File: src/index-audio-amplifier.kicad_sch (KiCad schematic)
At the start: 0 parts

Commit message: Add & associate `compact-title-block` submodule
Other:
- title: (none) -> Index Audio Amplifier
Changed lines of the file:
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@@
 	(generator_version "9.0")
 	(paper "A4")
+	(title_block
+		(title "Index Audio Amplifier")
+		(date "In-Progress")
+		(rev "0-dev")
+		(comment 1 "Peter S. Hollander")
+		(comment 2 "recursivenomad@protonmail.com")
+		(comment 3 "MIT-0 OR CC0-1.0")
+		(comment 4 "https://gitlab.com/recursivenomad/index-audio-amplifier/")
+	)
 	(sheet_instances
 		(path "/"

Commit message: Recreate Pico schematic (ignoring connectors)
<https://datasheets.raspberrypi.com/pico/pico-datasheet.pdf#pico-schematic-diagram>
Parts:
- added C1, C2: 47u, Capacitor_SMD:C_0805_2012Metric, symbol Device:C
- added C10, C11, C4, C5, C6, C7, C8, C9: 100n, Capacitor_SMD:C_0603_1608Metric, symbol Device:C
- added C12, C13, C14: 2u2, Capacitor_SMD:C_01005_0402Metric, symbol Device:C
- added C15: 100n, Capacitor_SMD:C_0402_1005Metric, symbol Device:C
- added C16, C17: 15p, Capacitor_SMD:C_0603_1608Metric, symbol Device:C
- added C18: 2u2, Capacitor_SMD:C_0402_1005Metric, symbol Device:C
- added C3: 1n, Capacitor_SMD:C_0603_1608Metric, symbol Device:C
- added D1: MBR120VLSFT1G, Diode_SMD:D_SOD-123F, symbol Diode:MBR1020VL
- added D2: Green, symbol Device:LED
- added J1: USB_B_Micro, symbol Connector:USB_B_Micro
- added L1: 2u2, symbol Device:L
- added Q1: DMG1012T, Package_TO_SOT_SMD:SOT-523, symbol Transistor_FET:DMG1012T
- added R1: 10K, Resistor_SMD:R_0402_1005Metric, symbol Device:R
- added R10: 5K6, Resistor_SMD:R_0402_1005Metric, symbol Device:R
- added R11, R14: 1K, Resistor_SMD:R_0402_1005Metric, symbol Device:R
- added R12, R13: 27R, Resistor_SMD:R_0603_1608Metric, symbol Device:R
- added R15, R4: NO-FIT, Resistor_SMD:R_0402_1005Metric, symbol Device:R
- added R2, R6, R8: 100K, Resistor_SMD:R_0402_1005Metric, symbol Device:R
- added R3: 470R, Resistor_SMD:R_0402_1005Metric, symbol Device:R
- added R5: 200K, Resistor_SMD:R_0402_1005Metric, symbol Device:R
- added R7: 200R, Resistor_SMD:R_0603_1608Metric, symbol Device:R
- added R9: 1R, Resistor_SMD:R_0402_1005Metric, symbol Device:R
- added SW1: SW_Push, symbol Switch:SW_Push
- added U1: RP2040, Package_DFN_QFN:QFN-56-1EP_7x7mm_P0.4mm_EP3.2x3.2mm, symbol MCU_RaspberryPi:RP2040
- added U2: RT6150B-33GQW, Package_DFN_QFN:WDFN-10-1EP_3x3mm_P0.5mm_EP1.8x2.5mm_ThermalVias, symbol Regulator_Switching:TPS63000
- added U3: W25Q16JVUXIQ, Package_SON:Winbond_USON-8-1EP_3x2mm_P0.5mm_EP0.2x1.6mm, symbol Memory_Flash:W25Q16JVSS
- added X1: 12MHz, symbol Device:Crystal_GND24
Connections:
- new net: L1.1, U2.4 (L1)
- new net: L1.2, U2.2 (L2)
- new net: J1.3 (D+), R12.1
- new net: R12.2, U1.47 (USB_DP)
- new net: D2.2 (A), R3.2
- new net: D1.2 (A), J1.1 (VBUS), R10.1
- new net: C3.1, Q1.2 (S), R5.2, R6.1
- new net: C16.1, R15.2, U1.20 (XIN), X1.1
- new net: R11.1, SW1.2
- new net: C17.1, R14.1, X1.3
- new net: R14.2, R15.1, U1.21 (XOUT)
- new net: R3.1, U1.37 (GPIO25)
- new net: J1.2 (D-), R13.1
- new net: R11.2, R4.1, U1.56 (QSPI_SS), U3.1 (~{CS})
- new net: R13.2, U1.46 (USB_DM)
- new net: Q1.3 (D), U1.41 (GPIO29_ADC3)
- new net: U1.51 (QSPI_SD3), U3.7 (~{HOLD}/~{RESET}/IO_{3})
- new net: U1.52 (QSPI_SCLK), U3.6 (CLK)
- new net: U1.53 (QSPI_SD0), U3.5 (DI/IO_{0})
- new net: U1.54 (QSPI_SD2), U3.3 (~{WP}/IO_{2})
- new net: U1.55 (QSPI_SD1), U3.2 (DO/IO_{1})
- new net +1V1: C11.1, C12.1, C9.1, U1.23 (DVDD), U1.45 (VREG_VOUT), U1.50 (DVDD)
- new net +3V3: C10.1, C14.1, C15.1, C18.1, C2.1, C4.1, C5.1, C6.1, C7.1, C8.1, Q1.1 (G), R4.2, R7.1, U1.1 (IOVDD), U1.10 (IOVDD), U1.22 (IOVDD), U1.33 (IOVDD), U1.42 (IOVDD), U1.44 (VREG_IN), U1.48 (USB_VDD), U1.49 (IOVDD), U2.1 (VOUT), U2.10 (FB), U3.8 (VCC)
- new net 3V3_EN: R2.2, U2.6 (EN)
- new net ADC_VREF: R7.2, R9.1
- new net AVDD: C13.1, R9.2, U1.43 (ADC_AVDD)
- new net GND: C1.2, C10.2, C11.2, C12.2, C13.2, C14.2, C15.2, C16.2, C17.2, C18.2, C2.2, C3.2, C4.2, C5.2, C6.2, C7.2, C8.2, C9.2, D2.1 (K), J1.5 (GND), J1.6 (Shield), R1.2, R6.2, R8.2, SW1.1, U1.19 (TESTEN), U1.57 (GND), U2.11 (PGND), U2.3 (PGND), U2.9 (GND), U3.4 (GND), X1.2, X1.4
- new net GPIO23: R8.1, U1.35 (GPIO23), U2.7 (PS/SYNC)
- new net GPIO24: R1.1, R10.2, U1.36 (GPIO24)
- new net VSYS: C1.1, D1.1 (K), R2.1, R5.1, U2.5 (VIN), U2.8 (VINA)
- no-connect marks 0 -> 25

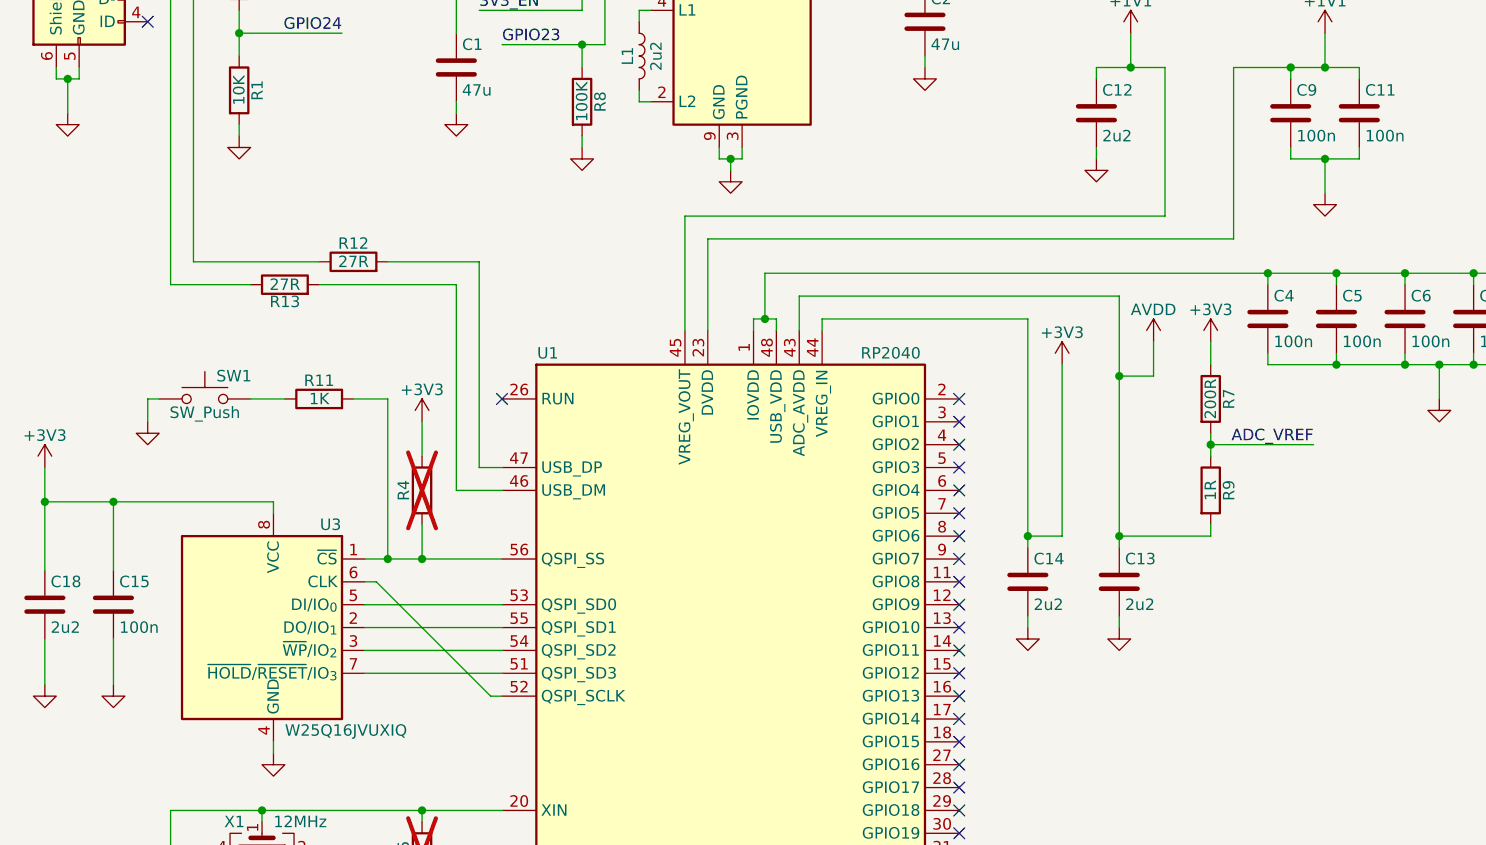
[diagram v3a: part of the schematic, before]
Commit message: Add discrete component proximity notes
Notes adopted from `RP2040_minimal_r2.kicad_pro` in "Minimal-KiCAD.zip"
from "Hardware design with RP2040":
<https://datasheets.raspberrypi.com/rp2040/hardware-design-with-rp2040.pdf#minimal-design-example>
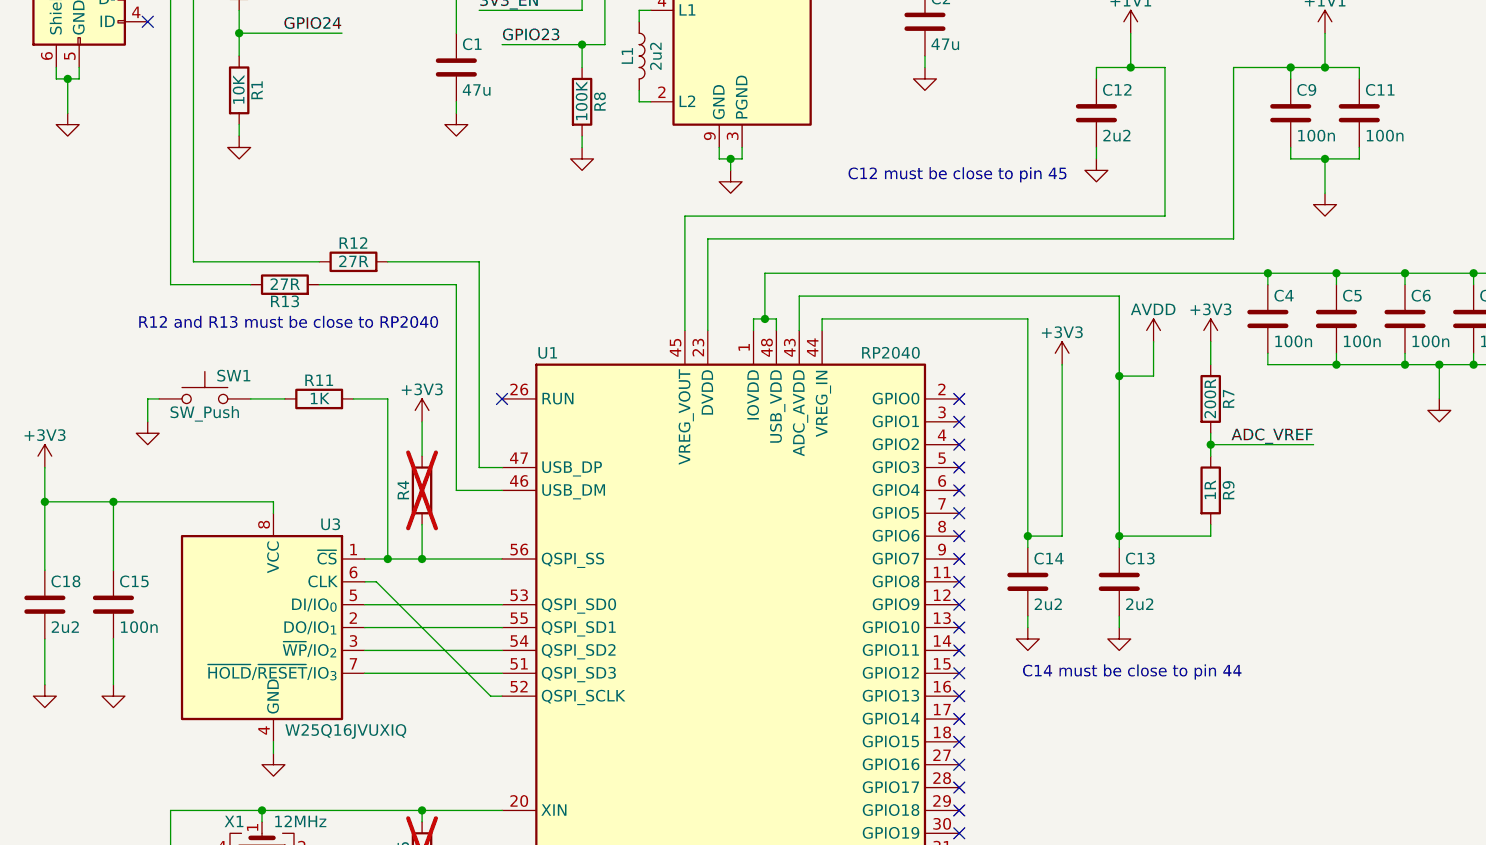
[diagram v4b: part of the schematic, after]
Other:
- note added: "C12 must be close to pin 45"
- note added: "C14 must be close to pin 44"
- note added: "R12 and R13 must be close to RP2040"
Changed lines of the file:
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@@
 		(comment 4 "https://gitlab.com/recursivenomad/index-audio-amplifier/")
+	)
+	(text "C14 must be close to pin 44"
+		(exclude_from_sim no)
+		(at 140.335 111.76 0)
+		(effects
+			(font
+				(size 1.27 1.27)
+			)
+			(justify left)
+		)
+	)
+	(text "R12 and R13 must be close to RP2040"
+		(exclude_from_sim no)
+		(at 75.565 73.025 0)
+		(effects
+			(font
+				(size 1.27 1.27)
+			)
+			(justify right)
+		)
+	)
+	(text "C12 must be close to pin 45"
+		(exclude_from_sim no)
+		(at 145.415 56.515 0)
+		(effects
+			(font
+				(size 1.27 1.27)
+			)
+			(justify right)
+		)
 	)
 	(junction

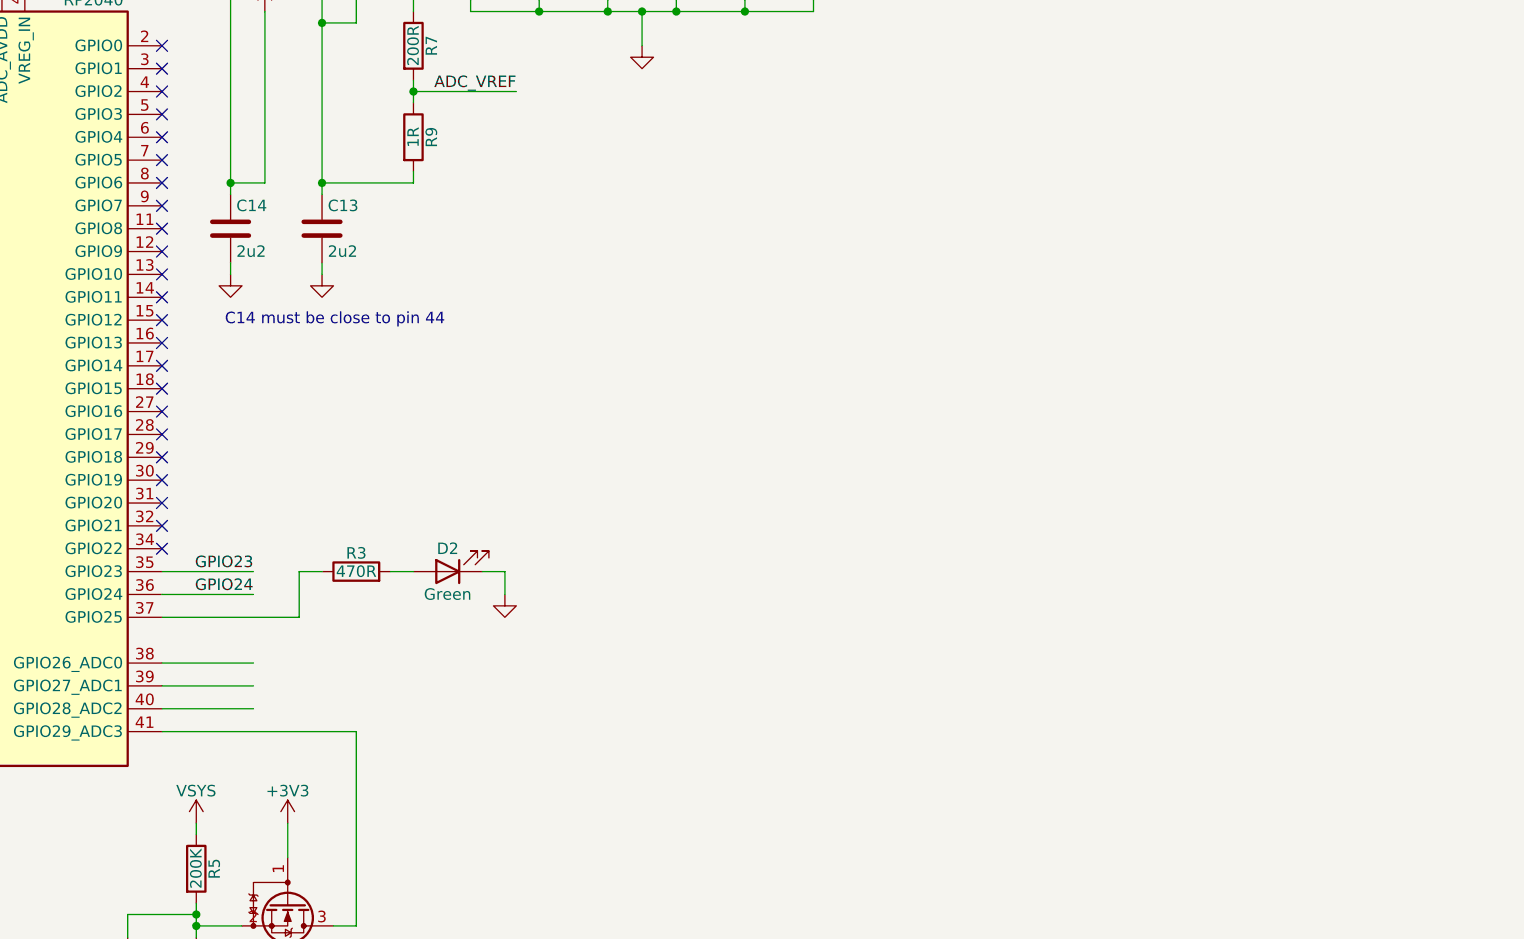
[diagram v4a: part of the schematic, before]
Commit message: Add PCM5101A for `usb_sound_card` firmware
Component selection adopted from `pico_vga_sd_aud.pro` in
"VGA_KiCAD.zip" from "Hardware design with RP2040":
<https://datasheets.raspberrypi.com/rp2040/hardware-design-with-rp2040.pdf#_the_vga_sd_card_audio_demo_boards_for_raspberry_pi_pico_and_raspberry_pi_pico_w>

Referenced firmware is on the branch `usb-sound-card` in the
index-audio-interface repository:
<https://gitlab.com/recursivenomad/index-audio-interface/-/tree/usb-sound-card/>

Which itself is rebased from Raspberry Pi's pico-playground repository:
<https://github.com/raspberrypi/pico-playground/tree/master/apps/usb_sound_card>
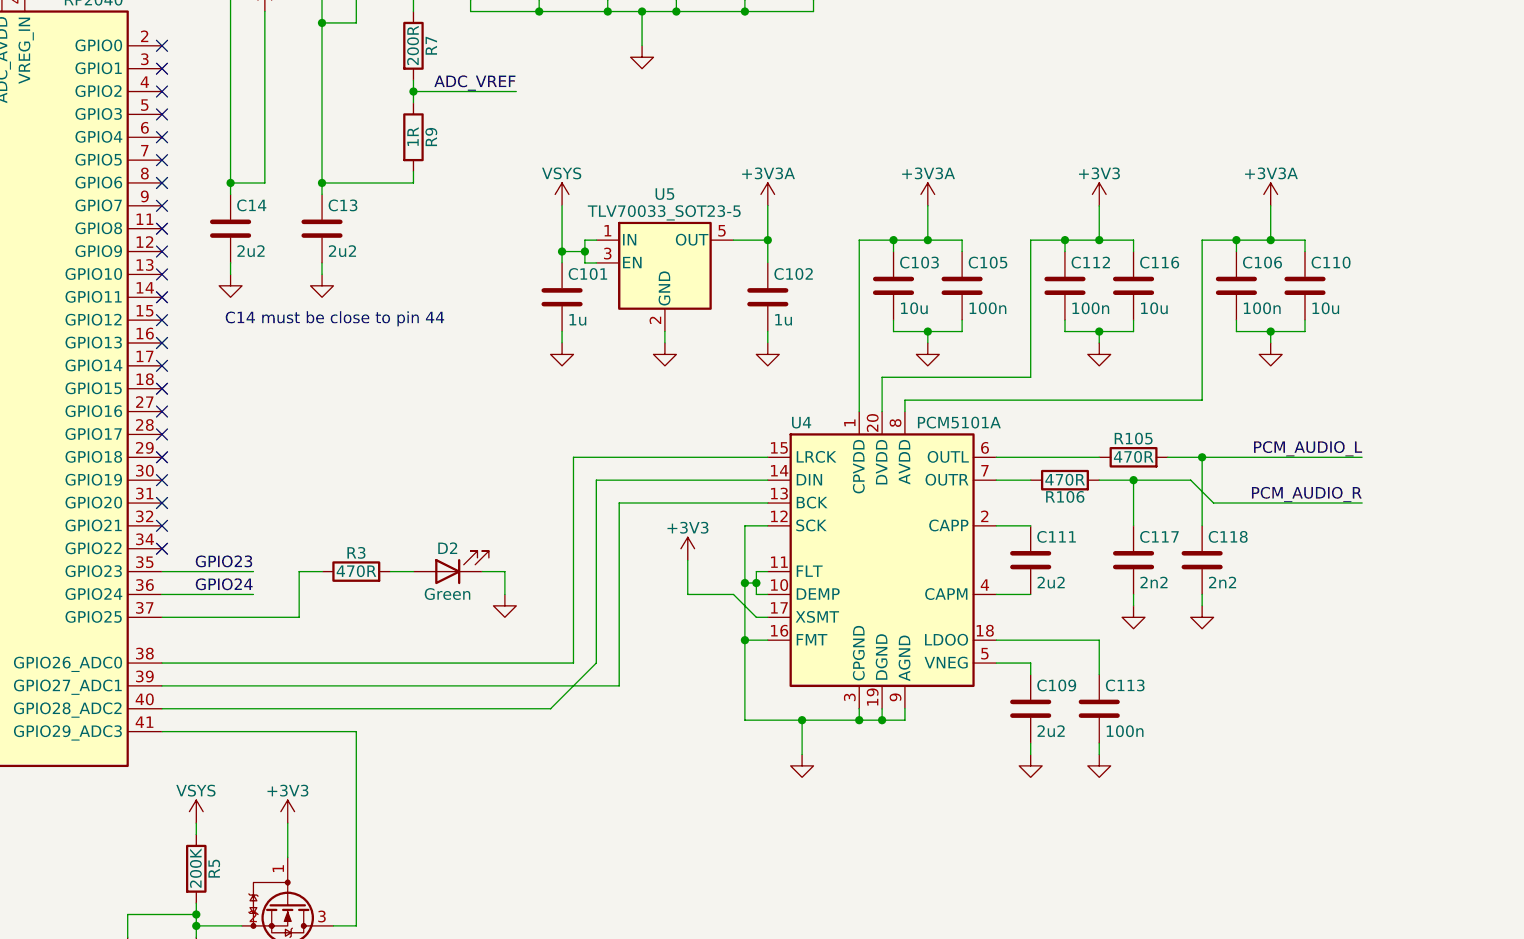
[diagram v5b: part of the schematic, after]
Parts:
- added C101, C102: 1u, Capacitor_SMD:C_01005_0402Metric, symbol Device:C
- added C103, C110, C116: 10u, Capacitor_SMD:C_01005_0402Metric, symbol Device:C
- added C105, C106, C112, C113: 100n, Capacitor_SMD:C_01005_0402Metric, symbol Device:C
- added C109, C111: 2u2, Capacitor_SMD:C_01005_0402Metric, symbol Device:C
- added C117, C118: 2n2, Capacitor_SMD:C_01005_0402Metric, symbol Device:C
- added R105, R106: 470R, Resistor_SMD:R_0402_1005Metric, symbol Device:R
- added U4: PCM5101A, Package_SO:TSSOP-20_4.4x6.5mm_P0.65mm, symbol Audio:PCM5101A
- added U5: TLV70033_SOT23-5, Package_TO_SOT_SMD:SOT-23-5, symbol Regulator_Linear:TLV70033_SOT23-5
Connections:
- net +3V3: now also C112.1, C116.1, U4.17 (XSMT), U4.20 (DVDD)
- net GND: now also C101.2, C102.2, C103.2, C105.2, C106.2, C109.2, C110.2, C112.2, C113.2, C116.2, C117.2, C118.2, U4.10 (DEMP), U4.11 (FLT), U4.12 (SCK), U4.16 (FMT), U4.19 (DGND), U4.3 (CPGND), U4.9 (AGND), U5.2 (GND)
- net VSYS: now also C101.1, U5.1 (IN), U5.3 (EN)
- net at U1.38 (GPIO26_ADC0): now also U4.15 (LRCK)
- net at U1.39 (GPIO27_ADC1): now also U4.13 (BCK)
- net at U1.40 (GPIO28_ADC2): now also U4.14 (DIN)
- new net: C113.1, U4.18 (LDOO)
- new net: R106.1, U4.7 (OUTR)
- new net: C111.1, U4.2 (CAPP)
- new net: C111.2, U4.4 (CAPM)
- new net: C109.1, U4.5 (VNEG)
- new net: R105.1, U4.6 (OUTL)
- new net +3V3A: C102.1, C103.1, C105.1, C106.1, C110.1, U4.1 (CPVDD), U4.8 (AVDD), U5.5 (OUT)
- new net PCM_AUDIO_L: C118.1, R105.2
- new net PCM_AUDIO_R: C117.1, R106.2
